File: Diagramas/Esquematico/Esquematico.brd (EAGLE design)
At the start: 70 x 100 mm, 48 parts, among them IC1 RASPBERRY_PI_ZERO_W_(V1.3), IC2 3071, IC3 DS3231N_DIP, J1 Modulo Pir, K1 SRD-05VDC-SL-C, K2 SRD-05VDC-SL-C, K3 SRD-05VDC-SL-C, K4 SRD-05VDC-SL-C, U1 RFM69HW-868S2

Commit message: modulo lora
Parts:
- moved IC2 16.5 mm to (24.9, 48.4)
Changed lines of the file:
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@@
 <attribute name="VALUE" x="33.8" y="83.8" size="1.27" layer="27" align="center"/>
 </element>
-<element name="IC2" library="3071" package="3071" value="3071" x="14.49" y="35.62" smashed="yes">
-<attribute name="ALLIED_NUMBER" value="70928125" x="119.9" y="-3.75" size="1.778" layer="27" display="off"/>
-<attribute name="ALLIED_PRICE-STOCK" value="https://www.alliedelec.com/adafruitindustries-3071/70928125/" x="119.9" y="-3.75" size="1.778" layer="27" display="off"/>
-<attribute name="DESCRIPTION" value="LoRa Packet Radio Breakout" x="119.9" y="-3.75" size="1.778" layer="27" display="off"/>
-<attribute name="HEIGHT" value="3.5mm" x="119.9" y="-3.75" size="1.778" layer="27" display="off"/>
-<attribute name="MANUFACTURER_NAME" value="Adafruit" x="119.9" y="-3.75" size="1.778" layer="27" display="off"/>
-<attribute name="MANUFACTURER_PART_NUMBER" value="3071" x="119.9" y="-3.75" size="1.778" layer="27" display="off"/>
-<attribute name="MOUSER_PART_NUMBER" value="485-3071" x="119.9" y="-3.75" size="1.778" layer="27" display="off"/>
-<attribute name="MOUSER_PRICE-STOCK" value="https://www.mouser.com/Search/Refine.aspx?Keyword=485-3071" x="119.9" y="-3.75" size="1.778" layer="27" display="off"/>
-<attribute name="NAME" x="24.65" y="48.32" size="1.27" layer="25" align="center"/>
-<attribute name="RS_PART_NUMBER" value="" x="119.9" y="-3.75" size="1.778" layer="27" display="off"/>
-<attribute name="RS_PRICE-STOCK" value="" x="119.9" y="-3.75" size="1.778" layer="27" display="off"/>
-<attribute name="VALUE" x="24.65" y="48.32" size="1.27" layer="27" align="center"/>
+<element name="IC2" library="3071" package="3071" value="3071" x="24.915" y="48.445" smashed="yes">
+<attribute name="ALLIED_NUMBER" value="70928125" x="130.325" y="9.075" size="1.778" layer="27" display="off"/>
+<attribute name="ALLIED_PRICE-STOCK" value="https://www.alliedelec.com/adafruitindustries-3071/70928125/" x="130.325" y="9.075" size="1.778" layer="27" display="off"/>
+<attribute name="DESCRIPTION" value="LoRa Packet Radio Breakout" x="130.325" y="9.075" size="1.778" layer="27" display="off"/>
+<attribute name="HEIGHT" value="3.5mm" x="130.325" y="9.075" size="1.778" layer="27" display="off"/>
+<attribute name="MANUFACTURER_NAME" value="Adafruit" x="130.325" y="9.075" size="1.778" layer="27" display="off"/>
+<attribute name="MANUFACTURER_PART_NUMBER" value="3071" x="130.325" y="9.075" size="1.778" layer="27" display="off"/>
+<attribute name="MOUSER_PART_NUMBER" value="485-3071" x="130.325" y="9.075" size="1.778" layer="27" display="off"/>
+<attribute name="MOUSER_PRICE-STOCK" value="https://www.mouser.com/Search/Refine.aspx?Keyword=485-3071" x="130.325" y="9.075" size="1.778" layer="27" display="off"/>
+<attribute name="NAME" x="35.075" y="61.145" size="1.27" layer="25" align="center"/>
+<attribute name="RS_PART_NUMBER" value="" x="130.325" y="9.075" size="1.778" layer="27" display="off"/>
+<attribute name="RS_PRICE-STOCK" value="" x="130.325" y="9.075" size="1.778" layer="27" display="off"/>
+<attribute name="VALUE" x="35.075" y="61.145" size="1.27" layer="27" align="center"/>
 </element>
 <element name="IC3" library="DS3231N_DIP" package="SOIC127P1032X265-16N" value="DS3231N_DIP" x="16.18" y="81.09" smashed="yes" rot="MR0">
@@
 <wire x1="5.28" y1="36.58" x2="5.23" y2="46.51" width="0" layer="19" extent="1-1"/>
 <wire x1="5.28" y1="26.665" x2="5.28" y2="36.58" width="0" layer="19" extent="1-1"/>
-<wire x1="5.28" y1="21.7" x2="5.28" y2="26.665" width="0" layer="19" extent="1-1"/>
-<wire x1="17.03" y1="35.62" x2="5.28" y2="36.58" width="0" layer="19" extent="1-1"/>
-<wire x1="20.98" y1="45.475" x2="17.03" y2="35.62" width="0" layer="19" extent="16-16"/>
-<wire x1="20.98" y1="48.015" x2="20.98" y2="45.475" width="0" layer="19" extent="16-16"/>
-<wire x1="20.98" y1="50.555" x2="20.98" y2="48.015" width="0" layer="19" extent="16-16"/>
-<wire x1="20.98" y1="53.095" x2="20.98" y2="50.555" width="0" layer="19" extent="16-16"/>
-<wire x1="18.515" y1="23.91" x2="17.03" y2="35.62" width="0" layer="19" extent="1-1"/>
+<wire x1="17.295" y1="35.745" x2="5.28" y2="26.665" width="0" layer="19" extent="1-1"/>
+<wire x1="5.28" y1="21.7" x2="17.295" y2="35.745" width="0" layer="19" extent="1-1"/>
+<wire x1="18.515" y1="23.91" x2="17.295" y2="35.745" width="0" layer="19" extent="1-1"/>
 <wire x1="14.995" y1="96.26" x2="11.468" y2="81.725" width="0" layer="19" extent="16-16"/>
+<wire x1="20.98" y1="53.095" x2="14.59" y2="66.63" width="0" layer="19" extent="16-16"/>
+<wire x1="20.98" y1="50.555" x2="20.98" y2="53.095" width="0" layer="19" extent="16-16"/>
+<wire x1="20.98" y1="48.015" x2="20.98" y2="50.555" width="0" layer="19" extent="16-16"/>
+<wire x1="20.98" y1="45.475" x2="20.98" y2="48.015" width="0" layer="19" extent="16-16"/>
 <wire x1="44.425" y1="47.54" x2="20.98" y2="48.015" width="0" layer="19" extent="16-16"/>
 <wire x1="46.965" y1="47.54" x2="44.425" y2="47.54" width="0" layer="19" extent="16-16"/>
@@
 <wire x1="17.265" y1="49.29" x2="17.21" y2="51.84" width="0" layer="19" extent="16-16"/>
 <wire x1="17.01" y1="46.74" x2="17.265" y2="49.29" width="0" layer="19" extent="16-16"/>
-<wire x1="14.49" y1="35.62" x2="17.01" y2="46.74" width="0" layer="19" extent="16-16"/>
+<wire x1="14.755" y1="35.745" x2="17.01" y2="46.74" width="0" layer="19" extent="16-16"/>
 </signal>
 <signal name="INT5">
@@
 <contactref element="IC1" pad="11"/>
 <contactref element="U1" pad="3"/>
-<wire x1="14.49" y1="61.02" x2="22.615" y2="93.72" width="0" layer="19" extent="1-1"/>
-<wire x1="46.17" y1="69.095" x2="14.49" y2="61.02" width="0" layer="19" extent="16-16"/>
+<wire x1="22.615" y1="93.72" x2="46.17" y2="69.095" width="0" layer="19" extent="16-16"/>
+<wire x1="14.755" y1="61.145" x2="46.17" y2="69.095" width="0" layer="19" extent="16-16"/>
 </signal>
 <signal name="G2">
@@
 <contactref element="U1" pad="4"/>
 <wire x1="44.17" y1="69.095" x2="30.235" y2="96.26" width="0" layer="19" extent="16-16"/>
-<wire x1="17.03" y1="61.02" x2="44.17" y2="69.095" width="0" layer="19" extent="16-16"/>
+<wire x1="17.295" y1="61.145" x2="44.17" y2="69.095" width="0" layer="19" extent="16-16"/>
 </signal>
 <signal name="G3">
@@
 <contactref element="U1" pad="5"/>
 <wire x1="42.17" y1="69.095" x2="40.395" y2="96.26" width="0" layer="19" extent="16-16"/>
-<wire x1="19.57" y1="61.02" x2="42.17" y2="69.095" width="0" layer="19" extent="16-16"/>
+<wire x1="19.835" y1="61.145" x2="42.17" y2="69.095" width="0" layer="19" extent="16-16"/>
 </signal>
 <signal name="G4">
 <contactref element="IC2" pad="11"/>
 <contactref element="U1" pad="6"/>
-<wire x1="22.11" y1="61.02" x2="40.17" y2="69.095" width="0" layer="19" extent="16-16"/>
+<wire x1="22.375" y1="61.145" x2="40.17" y2="69.095" width="0" layer="19" extent="16-16"/>
 </signal>
 <signal name="G5">
 <contactref element="IC2" pad="10"/>
 <contactref element="U1" pad="7"/>
-<wire x1="24.65" y1="61.02" x2="38.17" y2="69.095" width="0" layer="19" extent="16-16"/>
+<wire x1="24.915" y1="61.145" x2="38.17" y2="69.095" width="0" layer="19" extent="16-16"/>
 </signal>
 <signal name="CS">
 <contactref element="IC2" pad="8"/>
 <contactref element="U1" pad="15"/>
-<wire x1="32.27" y1="35.62" x2="48.17" y2="87.195" width="0" layer="19" extent="16-16"/>
+<wire x1="32.535" y1="35.745" x2="48.17" y2="87.195" width="0" layer="19" extent="16-16"/>
 </signal>
 <signal name="MOSI">
@@
 <contactref element="U1" pad="14"/>
 <wire x1="32.775" y1="93.72" x2="46.17" y2="87.195" width="0" layer="19" extent="16-16"/>
-<wire x1="29.73" y1="35.62" x2="46.17" y2="87.195" width="0" layer="19" extent="16-16"/>
+<wire x1="29.995" y1="35.745" x2="46.17" y2="87.195" width="0" layer="19" extent="16-16"/>
 </signal>
 <signal name="MISO">
@@
 <contactref element="U1" pad="13"/>
 <wire x1="35.315" y1="93.72" x2="44.17" y2="87.195" width="0" layer="19" extent="16-16"/>
-<wire x1="27.19" y1="35.62" x2="44.17" y2="87.195" width="0" layer="19" extent="16-16"/>
+<wire x1="27.455" y1="35.745" x2="44.17" y2="87.195" width="0" layer="19" extent="16-16"/>
 </signal>
 <signal name="SCK">
@@
 <contactref element="U1" pad="12"/>
 <wire x1="42.17" y1="87.195" x2="37.855" y2="93.72" width="0" layer="19" extent="16-16"/>
-<wire x1="24.65" y1="35.62" x2="42.17" y2="87.195" width="0" layer="19" extent="16-16"/>
+<wire x1="24.915" y1="35.745" x2="42.17" y2="87.195" width="0" layer="19" extent="16-16"/>
 </signal>
 <signal name="G0">
@@
 <contactref element="IC1" pad="7"/>
 <contactref element="U1" pad="2"/>
-<wire x1="22.11" y1="35.62" x2="48.17" y2="69.095" width="0" layer="19" extent="16-16"/>
 <wire x1="17.535" y1="93.72" x2="48.17" y2="69.095" width="0" layer="19" extent="16-16"/>
+<wire x1="22.375" y1="35.745" x2="48.17" y2="69.095" width="0" layer="19" extent="16-16"/>
 </signal>
 <signal name="EN">
 <contactref element="IC2" pad="3"/>
 <contactref element="IC1" pad="24"/>
-<wire x1="19.57" y1="35.62" x2="37.855" y2="96.26" width="0" layer="19" extent="1-1"/>
+<wire x1="19.835" y1="35.745" x2="37.855" y2="96.26" width="0" layer="19" extent="1-1"/>
 </signal>
 <signal name="N$2">
@@
 <contactref element="U1" pad="1"/>
 <contactref element="IC1" pad="15"/>
-<wire x1="34.81" y1="35.62" x2="50.17" y2="69.095" width="0" layer="19" extent="16-16"/>
 <wire x1="27.695" y1="93.72" x2="50.17" y2="69.095" width="0" layer="19" extent="16-16"/>
+<wire x1="35.075" y1="35.745" x2="50.17" y2="69.095" width="0" layer="19" extent="16-16"/>
 </signal>
 <signal name="RST_GSM">

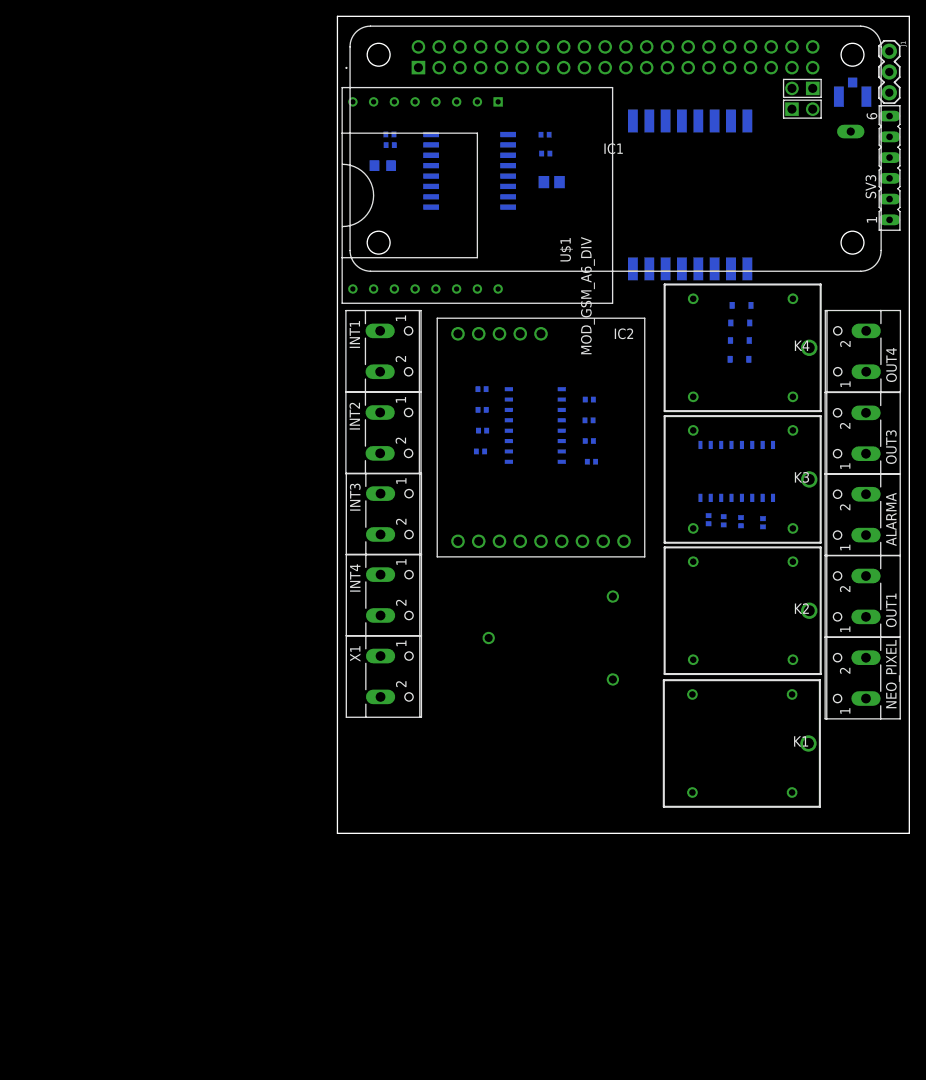
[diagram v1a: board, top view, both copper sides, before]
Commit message: Modulos en smd
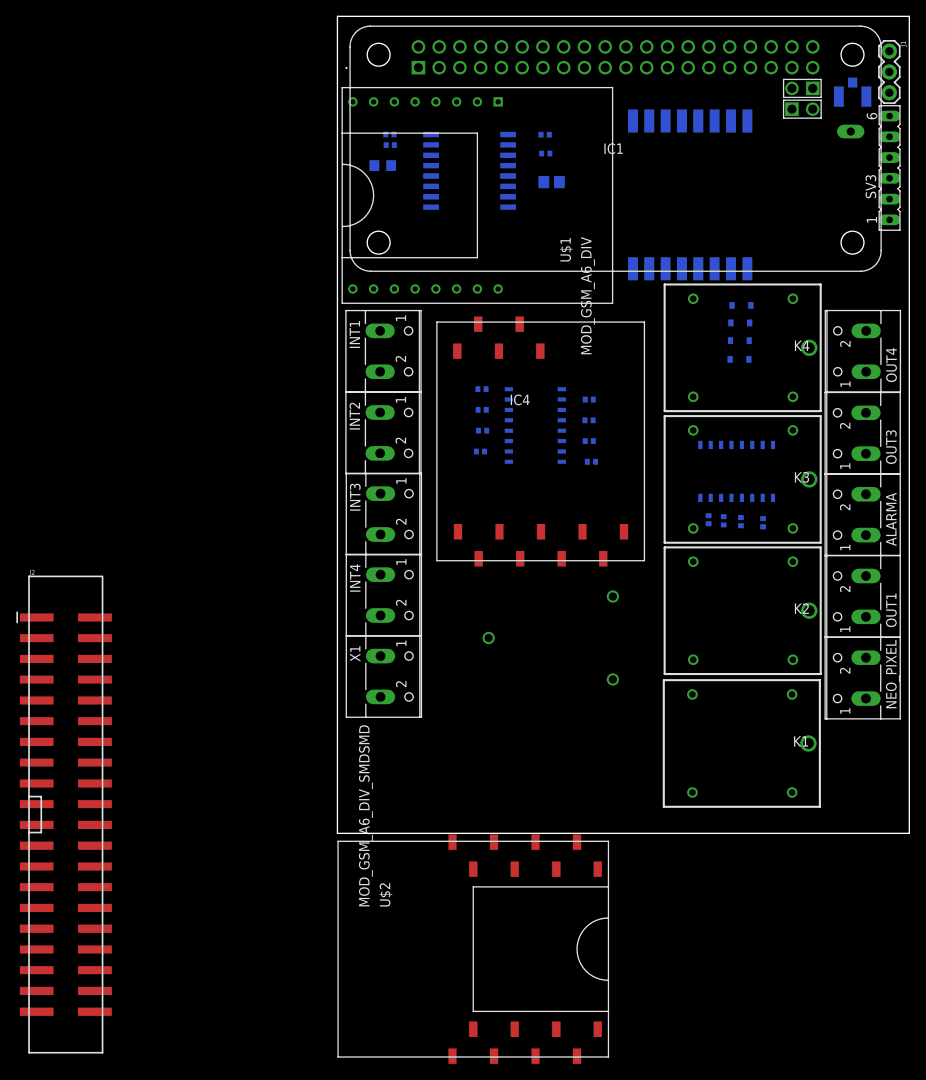
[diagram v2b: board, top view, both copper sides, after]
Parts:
- removed IC2: 3071, 3071:3071
- added IC4: 3071_SMD, 3071:3071_SMD
- added J2: RASPBERRYPI-40-PIN-GPIO_SMT, SparkFun-Connectors:2X20_SHROUDED_SMT
- added U$2: MOD_GSM_A6_DIV_SMDSMD, GPRS_A6 Mini:MOD_GSM_A6_SDM
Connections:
- new net N$50: U$2.HTX
- new net N$51: U$2.HRX
- new net N$52: U$2.GND
- new net N$53: U$2.URX
- new net N$54: U$2.UTX
- new net N$55: U$2.EAR_R
- new net N$56: U$2.EAR_L
- new net N$57: U$2.MIC2_P
- new net N$58: U$2.VCC
- new net N$59: U$2.IO14
- new net N$60: U$2.NETLED
- new net N$61: U$2.PWR
- new net N$62: U$2.INT
- new net N$63: U$2.RST
- new net N$64: U$2.MIC+
- new net N$65: U$2.MIC-
- net 3.3V: now also IC4.14, J2.1, J2.17; no longer IC2.1
- net 5V: now also J2.2, J2.4
- net CS: now also IC4.1; no longer IC2.8
- net EN: now also IC4.2; no longer IC2.3
- net G0: now also IC4.3; no longer IC2.4
- net G1: now also IC4.4; no longer IC2.14
- net G2: now also IC4.5; no longer IC2.13
- net G3: now also IC4.6; no longer IC2.12
- net G4: now also IC4.7; no longer IC2.11
- net G5: now also IC4.8; no longer IC2.10
- net GND: now also IC4.9, J2.14, J2.20, J2.25, J2.30, J2.34, J2.39, J2.6, J2.9; no longer IC2.2
- net MISO: now also IC4.10; no longer IC2.6
- net MOSI: now also IC4.11; no longer IC2.7
- net RST_LORA: now also IC4.12; no longer IC2.9
- net SCK: now also IC4.13; no longer IC2.5

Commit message: Acomo de coponentes
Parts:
- removed BT1: CR2032_MFR_RH, CR2032_MFR_RH:CR2032-MFR-RH
- removed IC1: RASPBERRY_PI_ZERO_W_(V1.3), Raspberry_Pi_Zero_W_(v1.3):RASPBERRYPIZEROWV13
- removed U$1: MOD_GSM_A6_DIV, GPRS_A6 Mini:MOD_GSM_A6
- added BT2: BU2032SM-BT-GTR, BU2032SM-BT-GTR:BAT_BU2032SM-BT-GTR
- moved J2 98.0 mm to (35.0, 72.6), flipped to the bottom, turned to 90 degrees
- moved U$2 79.2 mm to (17.5, 65.0), turned to 180 degrees
- moved ANT1 54.9 mm to (30.0, 46.3), turned to 270 degrees
- moved R14 49.8 mm to (29.5, 35.9), turned to 270 degrees
- moved R15 47.7 mm to (31.2, 35.9), turned to 270 degrees
- moved OK1 45.5 mm to (15.4, 5.28), turned to 90 degrees
- moved C3 43.8 mm to (33.7, 36.5), turned to 90 degrees
- moved R10 43.3 mm to (19.8, 11.1), turned to 90 degrees
- moved D1 41.8 mm to (50.0, 22.8)
- moved R11 40.7 mm to (17.3, 11.1), turned to 90 degrees
- moved K4 38.9 mm to (37.8, 26.0)
- moved R16 38.7 mm to (38.3, 63.7)
- moved C1 38.6 mm to (37.4, 59.9)
- moved R17 38.6 mm to (38.3, 62.4), turned to 180 degrees
- moved R12 38.2 mm to (14.7, 11.2), turned to 90 degrees
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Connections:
- removed net N$2: IC1.4
- removed net N$22: IC1.14
- removed net N$23: IC1.17
- removed net N$26: IC1.20
- removed net N$29: IC1.25
- removed net N$36: IC1.27
- removed net N$37: IC1.28
- removed net N$38: IC1.30
- removed net N$40: IC1.34
- removed net N$41: IC1.36
- removed net N$42: IC1.38
- removed net N$43: IC1.39
- removed net N$44: IC1.40
- removed net N$45: IC1.41
- removed net N$46: IC1.42
- removed net N$47: IC1.43
- removed net N$48: IC1.44
- removed net N$57: U$2.MIC2_P
- removed net N$58: U$2.VCC
- removed net N$59: U$2.IO14
- removed net N$60: U$2.NETLED
- removed net N$61: U$2.PWR
- removed net N$62: U$2.INT
- removed net N$63: U$2.RST
- removed net N$64: U$2.MIC+
- removed net N$65: U$2.MIC-
- removed net N$7: IC1.9
- new net N$14: J2.17
- new net N$25: J2.36
- new net N$30: J2.38
- new net N$31: J2.40
- new net N$6: J2.4
- net 3.3V: no longer IC1.1, J2.17
- net 5V: now also U$2.VCC; no longer IC1.2, J2.4, U$1.VCC
- net EAR_L: now also U$2.EAR_L; no longer U$1.EAR_L
- net EAR_R: now also U$2.EAR_R; no longer U$1.EAR_R
- net EN: now also J2.24; no longer IC1.24
- net G0: now also J2.7; no longer IC1.7
- net G1: now also J2.11; no longer IC1.11
- net G18: now also J2.12; no longer IC1.12
- net G2: now also J2.18; no longer IC1.18
- net G3: now also J2.26; no longer IC1.26
- net GND: now also BT2.2, U$2.GND; no longer BT1.3, IC1.6, J2.14, J2.20, J2.25, J2.30, J2.34, J2.39, J2.9, U$1.GND
- net HRX: now also U$2.HRX; no longer U$1.HRX
- net HTX: now also U$2.HTX; no longer U$1.HTX
- net INT: now also U$2.INT; no longer U$1.INT
- net INT1: now also J2.29; no longer IC1.29
- net INT2: now also J2.32; no longer IC1.32
- net INT3: now also J2.33; no longer IC1.33
- net INT4: now also J2.35; no longer IC1.35
- net INT5: now also J2.37; no longer IC1.37
- net IO14: now also U$2.IO14; no longer U$1.IO14
- net MIC+: now also U$2.MIC+; no longer U$1.MIC+
- net MIC-: now also U$2.MIC-; no longer U$1.MIC-
- net MIC2_P: now also U$2.MIC2_P; no longer U$1.MIC2_P
- net MISO: now also J2.21; no longer IC1.21
- net MOSI: now also J2.19; no longer IC1.19
- net N$50: now also J2.9; no longer U$2.HTX
- net N$51: now also J2.14; no longer U$2.HRX
- net N$52: now also J2.20; no longer U$2.GND
- net N$53: now also J2.25; no longer U$2.URX
- net N$54: now also J2.30; no longer U$2.UTX
- net N$55: now also J2.34; no longer U$2.EAR_R
- net N$56: now also J2.39; no longer U$2.EAR_L
- net NETLED: now also U$2.NETLED; no longer U$1.NETLED
- net OUT1: now also J2.16; no longer IC1.16
- net OUT3: now also J2.22; no longer IC1.22
- net OUT4: now also J2.31; no longer IC1.31
- net OUT_ALARMA: now also J2.13; no longer IC1.13
- net PWR: now also U$2.PWR; no longer U$1.PWR
- net RST_GSM: now also U$2.RST; no longer U$1.RST
- net RST_LORA: now also J2.15; no longer IC1.15
- net SCK: now also J2.23; no longer IC1.23
- net SCL: now also J2.5; no longer IC1.5
- net SDA: now also J2.3; no longer IC1.3
- net URX: now also J2.8, U$2.URX; no longer IC1.8, U$1.URX
- net UTX: now also J2.10, U$2.UTX; no longer IC1.10, U$1.UTX
- net VBAT: now also BT2.1; no longer BT1.1, BT1.2
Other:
- board size 70 x 100 mm -> 70 x 80.1 mm

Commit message: Ruteado de los componentes
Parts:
- moved J1 62.3 mm to (60.0, 12.0), turned to 90 degrees
- moved NEO_PIXEL 46.7 mm to (17.1, 6.20), turned to 0 degrees
- moved JP1 44.5 mm to (56.0, 34.2), turned to 0 degrees
- moved SV3 42.4 mm to (56.0, 18.4)
- moved R15 40.3 mm to (18.4, 74.1), flipped to the top, turned to 0 degrees
- moved OUT4 40.1 mm to (57.0, 6.20), turned to 0 degrees
- moved R14 39.2 mm to (21.0, 74.2), flipped to the top, turned to 180 degrees
- moved OUT1 38.0 mm to (27.1, 6.20), turned to 0 degrees
- moved OUT3 34.0 mm to (47.0, 6.20), turned to 0 degrees
- moved ALARMA 33.1 mm to (37.1, 6.20), turned to 0 degrees
- moved IC4 32.8 mm to (16.9, 65.5), turned to 270 degrees
- moved C3 32.2 mm to (49.9, 64.3), turned to 180 degrees
- moved ANT1 30.7 mm to (55.9, 29.7), turned to 90 degrees
- moved U$2 30.6 mm to (48.0, 63.1), turned to 90 degrees
- moved IC3 29.9 mm to (17.0, 64.1), flipped to the top, turned to 270 degrees
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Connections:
- net 5V: now also J1.2; no longer J1.3
- net INT5: now also J1.3; no longer J1.2
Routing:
- net GND: track 0.00 -> 340.5 mm, vias 0 -> 7
- net 5V: track 0.00 -> 196.3 mm, vias 0 -> 1
- net 3.3V: track 0.00 -> 186.8 mm, vias 0 -> 8
- net G18: track 0.00 -> 130.7 mm
- net SDA: track 0.00 -> 125.6 mm, vias 0 -> 4
- net CS: track 0.00 -> 107.5 mm, vias 0 -> 5
- net SCL: track 0.00 -> 95.7 mm, vias 0 -> 1
- net INT5: track 0.00 -> 89.7 mm, vias 0 -> 5
- net SQW: track 0.00 -> 85.4 mm, vias 0 -> 3
- net G3: track 0.00 -> 75.0 mm, vias 0 -> 5
- net N$34: track 0.00 -> 74.8 mm, vias 0 -> 2
- net G0: track 0.00 -> 71.8 mm, vias 0 -> 5
- net G1: track 0.00 -> 70.4 mm, vias 0 -> 7
- net INT2: track 0.00 -> 69.4 mm, vias 0 -> 2
- net INT3: track 0.00 -> 68.1 mm, vias 0 -> 4
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- added copper zone on layer 16, net GND
- added copper zone on layer 1, net GNG
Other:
- board size 70 x 80.1 mm -> 63.3 x 80.1 mm
- board text added: "+"
- board text added: "-"

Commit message: imagenes pcb
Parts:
- moved R6 0.72 mm to (8.64, 46.0)
- renumbered X1 to PWR
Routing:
- net SCL: track 95.7 -> 194.5 mm, vias 1 -> 6
- net N$34: track 74.8 -> 137.4 mm
- net SDA: track 125.6 -> 182.6 mm, vias 4 -> 7
- net INT5: track 89.7 -> 138.6 mm, vias 5 -> 2
- net G18: track 130.7 -> 97.0 mm, vias 0 -> 3
- net 3.3V: track 186.8 -> 217.6 mm, vias 8 -> 7
- net GND: track 340.5 -> 368.3 mm, vias 7 -> 5
- net CS: track 107.5 -> 80.4 mm, vias 5 -> 1
- net G1: track 70.4 -> 97.1 mm, vias 7 -> 5
- net N$10: track 7.50 -> 31.5 mm
- net OUT4: track 44.9 -> 65.9 mm
- net G3: track 75.0 -> 93.6 mm, vias 5 -> 6
- net G4: track 38.5 -> 52.7 mm
- net 5V: track 196.3 -> 183.3 mm
- net COM4: track 48.4 -> 61.0 mm, vias 0 -> 2
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- added copper zone on layer 1, net GND
- removed copper zone on layer 1, net GNG
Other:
- outline, holes or cut-outs redrawn
- board text added: "3.3V"
- board text added: "32K"
- board text added: "5V"
- board text added: "COM1"
- board text added: "COM2"
- board text added: "COM3"
- board text added: "COM4"
- board text added: "GND"
- board text added: "GP18"
- board text added: "INT1"
- board text added: "INT2"
- board text added: "INT3"
- board text added: "INT4"
- board text added: "INT5"
- board text added: "NO1"
- board text added: "NO2"
- board text added: "NO3"
- board text added: "NO4"
- board text added: "SCL"
- board text added: "SDA"
- board text added: "SQW"
